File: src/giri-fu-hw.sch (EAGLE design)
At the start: 30 parts, among them IC1 ATMEGA168-20P, IC2 7805T, IC3 ULN2003AN, K1 G5V1, K2 G5V1, K3 G5V1, K4 G5V1, K5 G5V1, K6 G5V1, Q1 16MHz

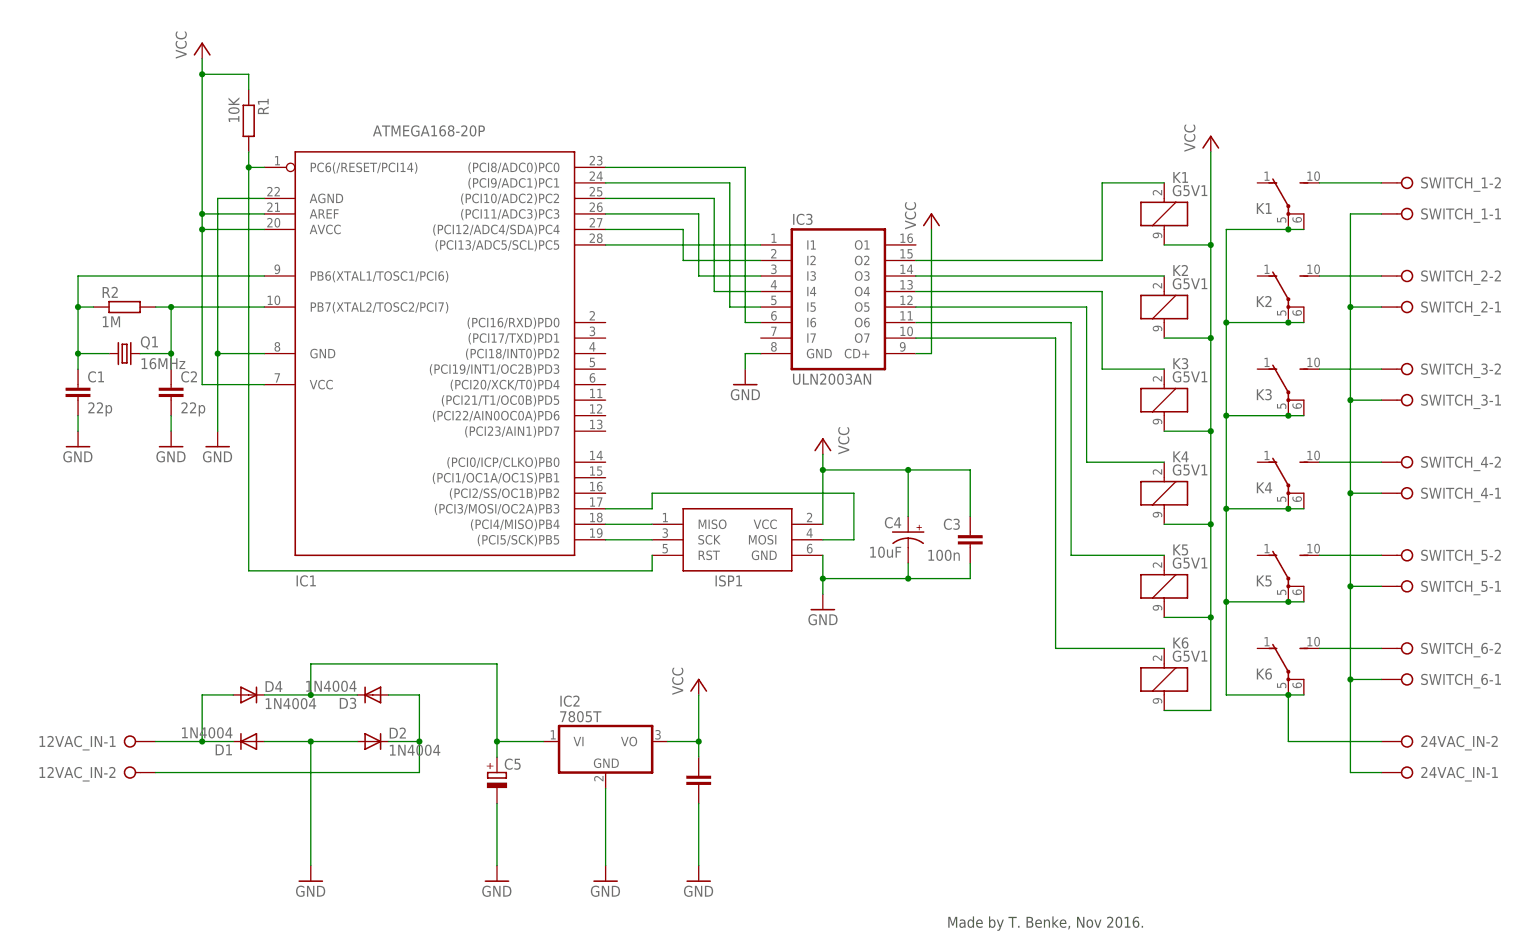
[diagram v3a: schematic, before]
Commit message: Add RS485 adapter
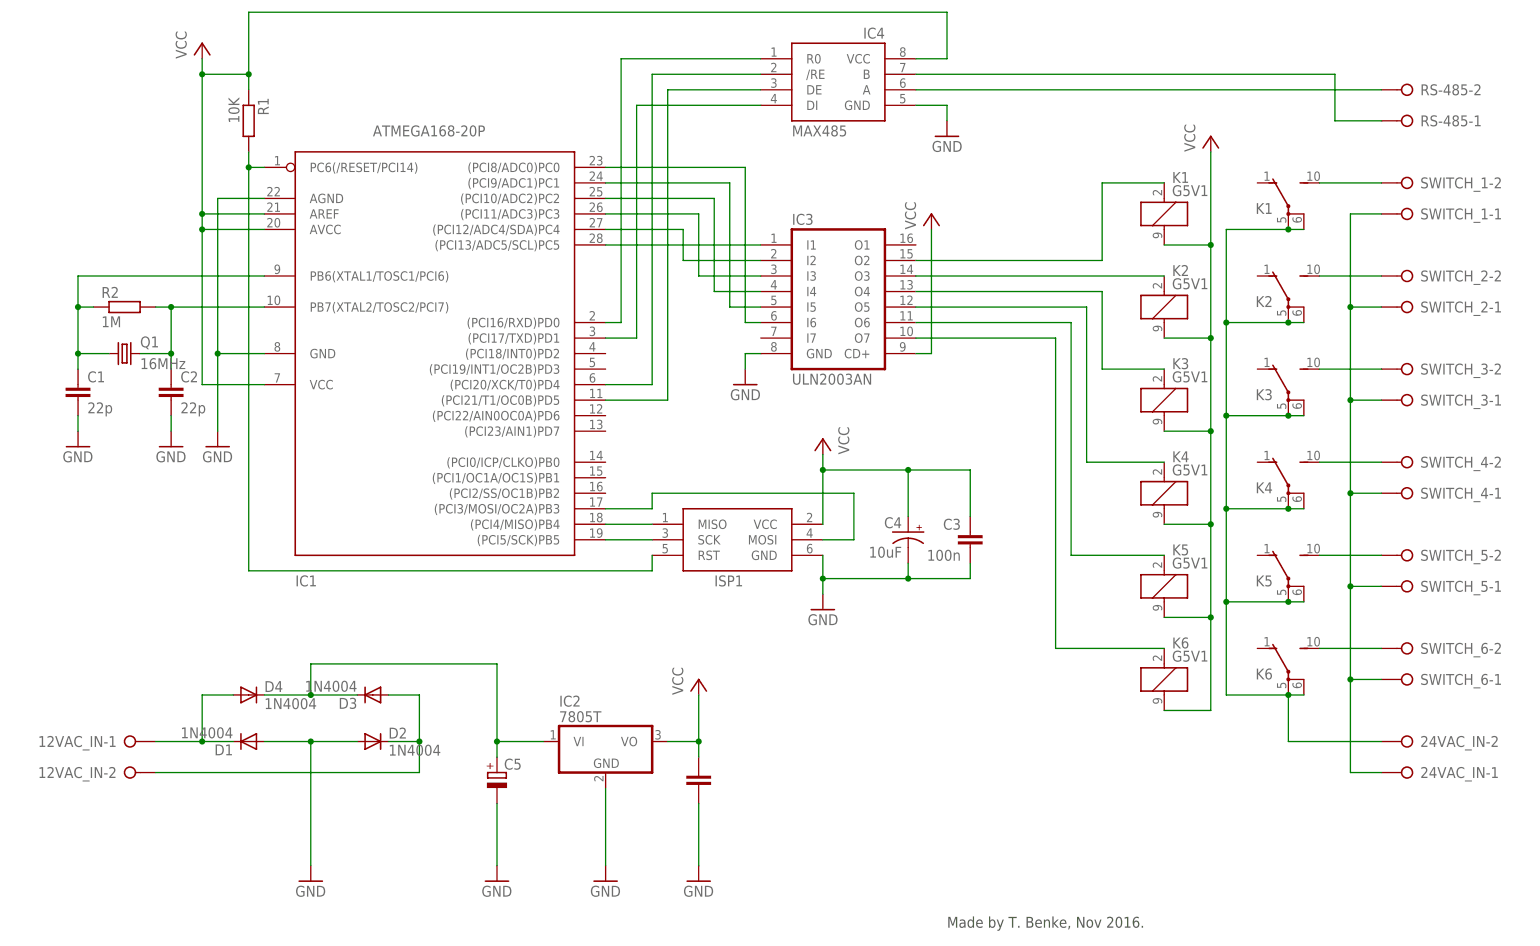
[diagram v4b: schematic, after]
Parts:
- added IC4: MAX485, max485:MAX485
- added RS-485: (no value), con-wago-508:W237-02P
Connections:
- new net N$24: IC4.A, RS-485-2.KL
- new net N$25: IC4.B, RS-485-1.KL
- new net N$26: IC1.(PCI16/RXD)PD0, IC4.R0
- new net N$27: IC1.(PCI17/TXD)PD1, IC4.DI
- new net N$36: IC1.(PCI20/XCK/T0)PD4, IC4./RE
- new net N$38: IC1.(PCI21/T1/OC0B)PD5, IC4.DE
- net GND: now also IC4.GND
- net N$8: now also IC4.VCC
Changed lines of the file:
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@@
 <part name="P+4" library="supply1" deviceset="VCC" device=""/>
 <part name="P+5" library="supply1" deviceset="VCC" device=""/>
+<part name="RS-485" library="con-wago-508" deviceset="W237-02P" device=""/>
+<part name="IC4" library="max485" deviceset="MAX485" device=""/>
+<part name="GND6" library="supply1" deviceset="GND" device=""/>
 </parts>
 <sheets>
@@
 <instance part="P+4" gate="VCC" x="121.92" y="60.96"/>
 <instance part="P+5" gate="VCC" x="205.74" y="149.86"/>
+<instance part="RS-485" gate="-1" x="238.76" y="152.4" rot="R180"/>
+<instance part="RS-485" gate="-2" x="238.76" y="157.48" rot="R180"/>
+<instance part="IC4" gate="G$1" x="142.24" y="160.02"/>
+<instance part="GND6" gate="1" x="162.56" y="149.86" rot="MR0"/>
 </instances>
 <busses>
@@
 <pinref part="GND13" gate="1" pin="GND"/>
 <wire x1="121.92" y1="30.48" x2="121.92" y2="40.64" width="0.1524" layer="91"/>
+</segment>
+<segment>
+<pinref part="IC4" gate="G$1" pin="GND"/>
+<pinref part="GND6" gate="1" pin="GND"/>
+<wire x1="157.48" y1="154.94" x2="162.56" y2="154.94" width="0.1524" layer="91"/>
+<wire x1="162.56" y1="154.94" x2="162.56" y2="152.4" width="0.1524" layer="91"/>
 </segment>
 </net>
@@
 <wire x1="48.26" y1="160.02" x2="40.64" y2="160.02" width="0.1524" layer="91"/>
 <junction x="40.64" y="160.02"/>
+<pinref part="IC4" gate="G$1" pin="VCC"/>
+<wire x1="157.48" y1="162.56" x2="162.56" y2="162.56" width="0.1524" layer="91"/>
+<wire x1="162.56" y1="162.56" x2="162.56" y2="170.18" width="0.1524" layer="91"/>
+<wire x1="162.56" y1="170.18" x2="48.26" y2="170.18" width="0.1524" layer="91"/>
+<wire x1="48.26" y1="170.18" x2="48.26" y2="160.02" width="0.1524" layer="91"/>
+<junction x="48.26" y="160.02"/>
 </segment>
 <segment>
@@
 </segment>
 </net>
+<net name="N$26" class="0">
+<segment>
+<pinref part="IC1" gate="G$1" pin="(PCI16/RXD)PD0"/>
+<wire x1="106.68" y1="119.38" x2="109.22" y2="119.38" width="0.1524" layer="91"/>
+<wire x1="109.22" y1="119.38" x2="109.22" y2="162.56" width="0.1524" layer="91"/>
+<pinref part="IC4" gate="G$1" pin="R0"/>
+<wire x1="109.22" y1="162.56" x2="132.08" y2="162.56" width="0.1524" layer="91"/>
+</segment>
+</net>
+<net name="N$27" class="0">
+<segment>
+<pinref part="IC1" gate="G$1" pin="(PCI17/TXD)PD1"/>
+<wire x1="106.68" y1="116.84" x2="111.76" y2="116.84" width="0.1524" layer="91"/>
+<wire x1="111.76" y1="116.84" x2="111.76" y2="154.94" width="0.1524" layer="91"/>
+<pinref part="IC4" gate="G$1" pin="DI"/>
+<wire x1="111.76" y1="154.94" x2="132.08" y2="154.94" width="0.1524" layer="91"/>
+</segment>
+</net>
+<net name="N$36" class="0">
+<segment>
+<pinref part="IC1" gate="G$1" pin="(PCI20/XCK/T0)PD4"/>
+<wire x1="106.68" y1="109.22" x2="114.3" y2="109.22" width="0.1524" layer="91"/>
+<wire x1="114.3" y1="109.22" x2="114.3" y2="160.02" width="0.1524" layer="91"/>
+<pinref part="IC4" gate="G$1" pin="/RE"/>
+<wire x1="114.3" y1="160.02" x2="132.08" y2="160.02" width="0.1524" layer="91"/>
+</segment>
+</net>
+<net name="N$38" class="0">
+<segment>
+<pinref part="IC1" gate="G$1" pin="(PCI21/T1/OC0B)PD5"/>
+<wire x1="106.68" y1="106.68" x2="116.84" y2="106.68" width="0.1524" layer="91"/>
+<wire x1="116.84" y1="106.68" x2="116.84" y2="157.48" width="0.1524" layer="91"/>
+<pinref part="IC4" gate="G$1" pin="DE"/>
+<wire x1="116.84" y1="157.48" x2="132.08" y2="157.48" width="0.1524" layer="91"/>
+</segment>
+</net>
+<net name="N$24" class="0">
+<segment>
+<pinref part="IC4" gate="G$1" pin="A"/>
+<pinref part="RS-485" gate="-2" pin="KL"/>
+<wire x1="157.48" y1="157.48" x2="233.68" y2="157.48" width="0.1524" layer="91"/>
+</segment>
+</net>
+<net name="N$25" class="0">
+<segment>
+<pinref part="IC4" gate="G$1" pin="B"/>
+<wire x1="157.48" y1="160.02" x2="226.06" y2="160.02" width="0.1524" layer="91"/>
+<wire x1="226.06" y1="160.02" x2="226.06" y2="152.4" width="0.1524" layer="91"/>
+<pinref part="RS-485" gate="-1" pin="KL"/>
+<wire x1="226.06" y1="152.4" x2="233.68" y2="152.4" width="0.1524" layer="91"/>
+</segment>
+</net>
